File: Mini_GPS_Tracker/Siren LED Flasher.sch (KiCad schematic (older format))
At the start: 16 parts, among them IC3 MIC2288YML-TR, J6 Siren 12V, Q2 2N2219

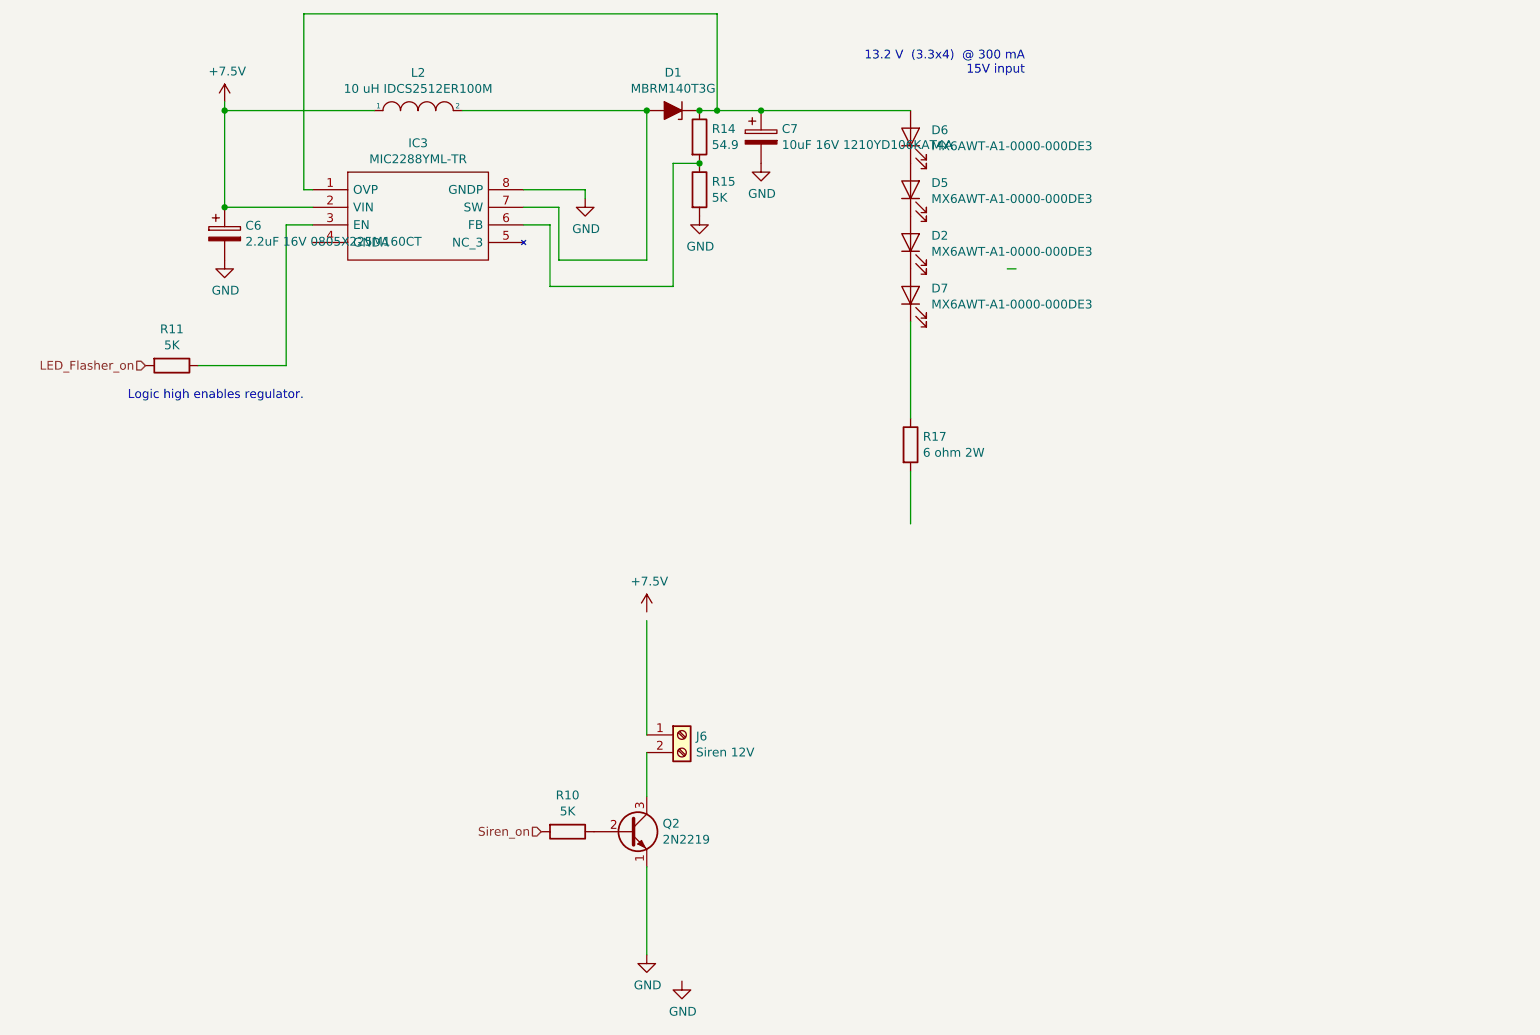
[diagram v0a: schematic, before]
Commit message: Add files via upload
More changes - USB, WiFi/BT, Buzzer, Siren-LED Flasher
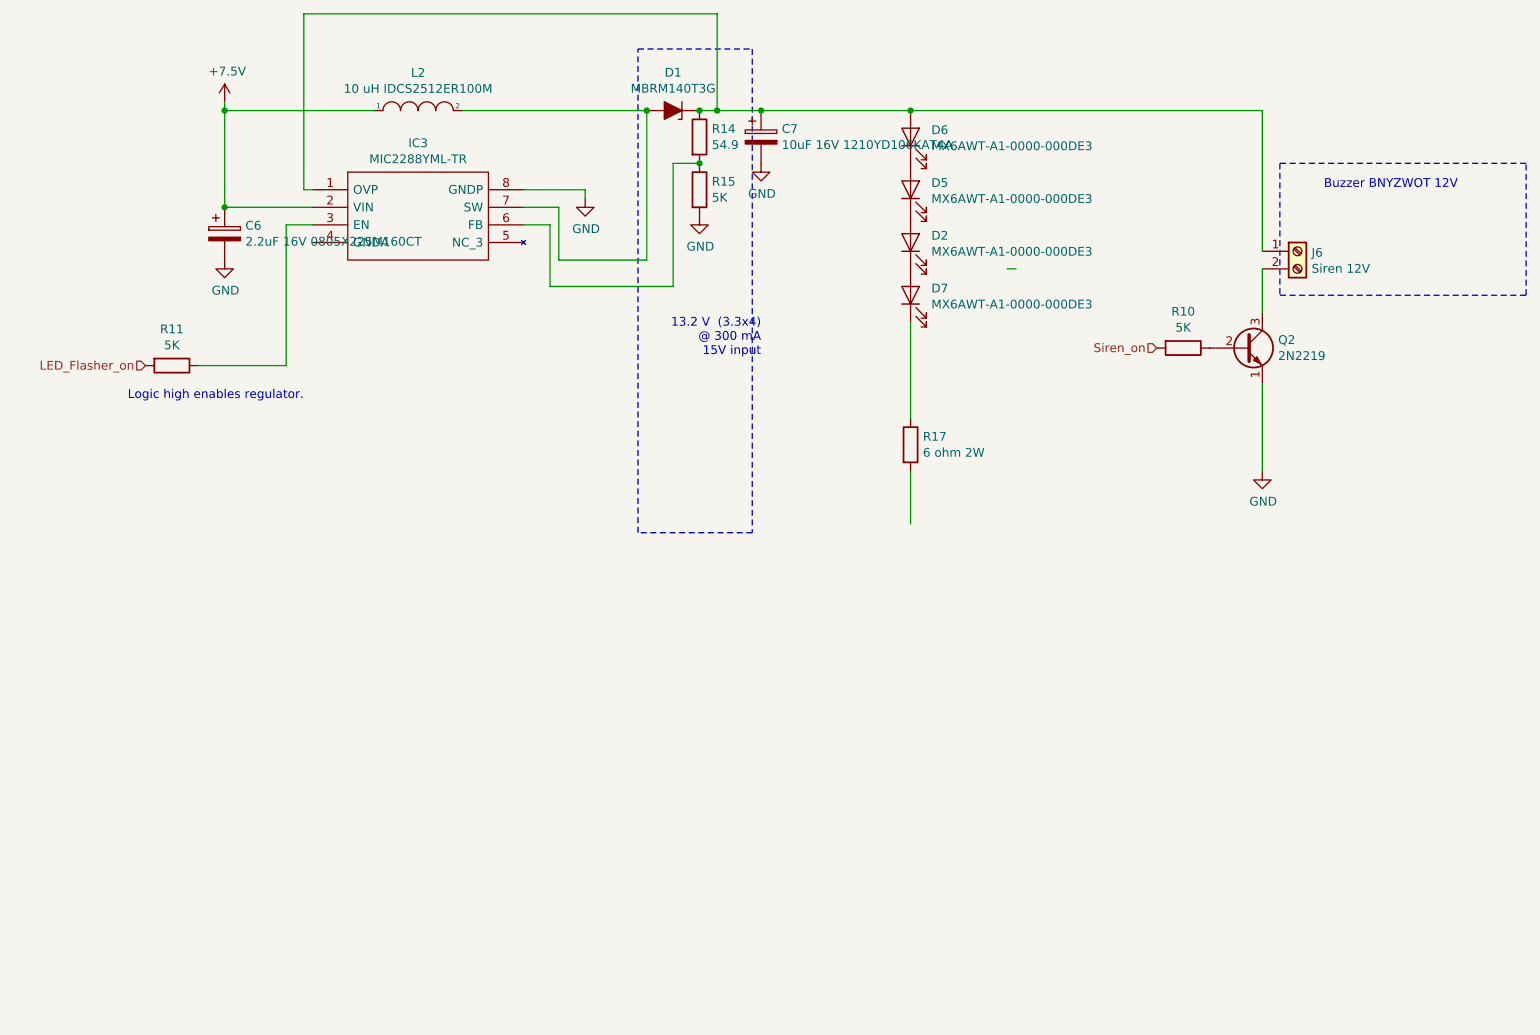
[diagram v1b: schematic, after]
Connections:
- wire segments 32 -> 33
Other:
- note added: "13.2 V (3.3x4) \n@ 300 mA\n15V input"
- note added: "Buzzer BNYZWOT 12V"
- note removed: "13.2 V (3.3x4) @ 300 mA\n15V input"
- moved on the sheet: J6, Q2, R10
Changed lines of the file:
@@
 Comment4 ""
 $EndDescr
-Text HLabel 5000 6000 0    50   Input ~ 0
+Text HLabel 8500 3250 0    50   Input ~ 0
 Siren_on
 Text HLabel 2750 3350 0    50   Input ~ 0
@@
 	1    4300 1900
 	1    0    0    -1
-$EndComp
-$Comp
-L Device:D_Zener_ALT D1
-U 1 1 5EB4CEF1
-P 5750 1900
-F 0 "D1" H 5750 1684 50  0000 C CNN
-F 1 "MBRM140T3G" H 5750 1775 50  0000 C CNN
-F 2 "" H 5750 1900 50  0001 C CNN
-F 3 "~" H 5750 1900 50  0001 C CNN
-	1    5750 1900
-	-1   0    0    1
 $EndComp
 $Comp
@@
 	5600 2750 5600 1900
 Wire Wire Line
-	5600 1900 4550 1900
-Wire Wire Line
 	3200 2450 3200 1900
 Wire Wire Line
 	3200 1900 4050 1900
-Connection ~ 5600 1900
-$Comp
-L Device:R R14
-U 1 1 5EB577A0
-P 5900 2050
-F 0 "R14" H 5970 2096 50  0000 L CNN
-F 1 "54.9" H 5970 2005 50  0000 L CNN
-F 2 "" V 5830 2050 50  0001 C CNN
-F 3 "~" H 5900 2050 50  0001 C CNN
-	1    5900 2050
-	1    0    0    -1
-$EndComp
-$Comp
-L Device:R R15
-U 1 1 5EB59096
-P 5900 2350
-F 0 "R15" H 5970 2396 50  0000 L CNN
-F 1 "5K" H 5970 2305 50  0000 L CNN
-F 2 "" V 5830 2350 50  0001 C CNN
-F 3 "~" H 5900 2350 50  0001 C CNN
-	1    5900 2350
-	1    0    0    -1
-$EndComp
-$Comp
-L power:GND #PWR060
-U 1 1 5EB59319
-P 5900 2500
-F 0 "#PWR060" H 5900 2250 50  0001 C CNN
-F 1 "GND" H 5905 2327 50  0000 C CNN
-F 2 "" H 5900 2500 50  0001 C CNN
-F 3 "" H 5900 2500 50  0001 C CNN
-	1    5900 2500
-	1    0    0    -1
-$EndComp
 Wire Wire Line
 	4900 2550 5050 2550
@@
 	5750 2900 5750 2200
 Wire Wire Line
-	5750 2200 5900 2200
-Connection ~ 5900 2200
-Wire Wire Line
 	5900 1900 6000 1900
-Connection ~ 5900 1900
 $Comp
 L Device:CP C6
@@
 	0    -1   -1   0
 $EndComp
-Text Notes 7750 1700 2    50   ~ 0
-13.2 V  (3.3x4)  @ 300 mA\n15V input
+Text Notes 6250 3300 2    50   ~ 0
+13.2 V  (3.3x4)  \n@ 300 mA\n15V input
 $Comp
 L Connector:Screw_Terminal_01x02 J6
 U 1 1 5EB7C544
-P 5800 5450
-F 0 "J6" H 5880 5442 50  0000 L CNN
-F 1 "Siren 12V" H 5880 5351 50  0000 L CNN
-F 2 "" H 5800 5450 50  0001 C CNN
-F 3 "~" H 5800 5450 50  0001 C CNN
-	1    5800 5450
+P 9300 2700
+F 0 "J6" H 9380 2692 50  0000 L CNN
+F 1 "Siren 12V" H 9380 2601 50  0000 L CNN
+F 2 "" H 9300 2700 50  0001 C CNN
+F 3 "~" H 9300 2700 50  0001 C CNN
+	1    9300 2700
 	1    0    0    -1
 $EndComp
@@
 	3650 1350 3650 2350
 $Comp
-L power:GND #PWR063
-U 1 1 5EB84950
-P 5800 6850
-F 0 "#PWR063" H 5800 6600 50  0001 C CNN
-F 1 "GND" H 5805 6677 50  0000 C CNN
-F 2 "" H 5800 6850 50  0001 C CNN
-F 3 "" H 5800 6850 50  0001 C CNN
-	1    5800 6850
-	1    0    0    -1
-$EndComp
-$Comp
 L Device:R R10
 U 1 1 5EB9F7A7
-P 5150 6000
-F 0 "R10" V 4943 6000 50  0000 C CNN
-F 1 "5K" V 5034 6000 50  0000 C CNN
-F 2 "" V 5080 6000 50  0001 C CNN
-F 3 "~" H 5150 6000 50  0001 C CNN
-	1    5150 6000
+P 8650 3250
+F 0 "R10" V 8443 3250 50  0000 C CNN
+F 1 "5K" V 8534 3250 50  0000 C CNN
+F 2 "" V 8580 3250 50  0001 C CNN
+F 3 "~" H 8650 3250 50  0001 C CNN
+	1    8650 3250
 	0    1    1    0
 $EndComp
@@
 L Transistor_BJT:2N2219 Q2
 U 1 1 5EBBDCB1
-P 5500 6000
-F 0 "Q2" H 5690 6046 50  0000 L CNN
-F 1 "2N2219" H 5690 5955 50  0000 L CNN
-F 2 "Package_TO_SOT_THT:TO-39-3" H 5700 5925 50  0001 L CIN
-F 3 "http://www.onsemi.com/pub_link/Collateral/2N2219-D.PDF" H 5500 6000 50  0001 L CNN
-	1    5500 6000
-	1    0    0    -1
-$EndComp
-Wire Wire Line
-	5600 4800 5600 5450
-Wire Wire Line
-	5600 5550 5600 5800
+P 9000 3250
+F 0 "Q2" H 9190 3296 50  0000 L CNN
+F 1 "2N2219" H 9190 3205 50  0000 L CNN
+F 2 "Package_TO_SOT_THT:TO-39-3" H 9200 3175 50  0001 L CIN
+F 3 "http://www.onsemi.com/pub_link/Collateral/2N2219-D.PDF" H 9000 3250 50  0001 L CNN
+	1    9000 3250
+	1    0    0    -1
+$EndComp
+Wire Wire Line
+	9100 2800 9100 3050
 Wire Wire Line
 	7100 3100 7100 3650
-$Comp
-L power:+7.5V #PWR053
-U 1 1 5EBC5061
-P 5600 4750
-F 0 "#PWR053" H 5600 4600 50  0001 C CNN
-F 1 "+7.5V" H 5615 4923 50  0000 C CNN
-F 2 "" H 5600 4750 50  0001 C CNN
-F 3 "" H 5600 4750 50  0001 C CNN
-	1    5600 4750
-	1    0    0    -1
-$EndComp
 $Comp
 L power:GND #PWR054
 U 1 1 5EBC5759
-P 5600 6700
-F 0 "#PWR054" H 5600 6450 50  0001 C CNN
-F 1 "GND" H 5605 6527 50  0000 C CNN
-F 2 "" H 5600 6700 50  0001 C CNN
-F 3 "" H 5600 6700 50  0001 C CNN
-	1    5600 6700
-	1    0    0    -1
-$EndComp
-Wire Wire Line
-	5600 6200 5600 6700
+P 9100 3950
+F 0 "#PWR054" H 9100 3700 50  0001 C CNN
+F 1 "GND" H 9105 3777 50  0000 C CNN
+F 2 "" H 9100 3950 50  0001 C CNN
+F 3 "" H 9100 3950 50  0001 C CNN
+	1    9100 3950
+	1    0    0    -1
+$EndComp
+Wire Wire Line
+	9100 3450 9100 3950
+Connection ~ 5900 1900
+Connection ~ 5600 1900
+Wire Wire Line
+	5600 1900 4550 1900
+Connection ~ 5900 2200
+Wire Wire Line
+	5750 2200 5900 2200
+$Comp
+L power:GND #PWR060
+U 1 1 5EB59319
+P 5900 2500
+F 0 "#PWR060" H 5900 2250 50  0001 C CNN
+F 1 "GND" H 5905 2327 50  0000 C CNN
+F 2 "" H 5900 2500 50  0001 C CNN
+F 3 "" H 5900 2500 50  0001 C CNN
+	1    5900 2500
+	1    0    0    -1
+$EndComp
+$Comp
+L Device:R R15
+U 1 1 5EB59096
+P 5900 2350
+F 0 "R15" H 5970 2396 50  0000 L CNN
+F 1 "5K" H 5970 2305 50  0000 L CNN
+F 2 "" V 5830 2350 50  0001 C CNN
+F 3 "~" H 5900 2350 50  0001 C CNN
+	1    5900 2350
+	1    0    0    -1
+$EndComp
+$Comp
+L Device:R R14
+U 1 1 5EB577A0
+P 5900 2050
+F 0 "R14" H 5970 2096 50  0000 L CNN
+F 1 "54.9" H 5970 2005 50  0000 L CNN
+F 2 "" V 5830 2050 50  0001 C CNN
+F 3 "~" H 5900 2050 50  0001 C CNN
+	1    5900 2050
+	1    0    0    -1
+$EndComp
+$Comp
+L Device:D_Zener_ALT D1
+U 1 1 5EB4CEF1
+P 5750 1900
+F 0 "D1" H 5750 1684 50  0000 C CNN
+F 1 "MBRM140T3G" H 5750 1775 50  0000 C CNN
+F 2 "" H 5750 1900 50  0001 C CNN
+F 3 "~" H 5750 1900 50  0001 C CNN
+	1    5750 1900
+	-1   0    0    1
+$EndComp
+Wire Notes Line
+	6200 1550 6200 4300
+Wire Notes Line
+	6200 4300 5550 4300
+Wire Notes Line
+	5550 4300 5550 1550
+Wire Notes Line
+	5550 1550 6200 1550
+Wire Notes Line
+	9200 2950 10600 2950
+Wire Notes Line
+	10600 2950 10600 2200
+Wire Notes Line
+	10600 2200 9200 2200
+Wire Notes Line
+	9200 2200 9200 2950
+Text Notes 9450 2350 0    50   ~ 0
+Buzzer BNYZWOT 12V
+Wire Wire Line
+	7100 1900 9100 1900
+Wire Wire Line
+	9100 1900 9100 2700
+Connection ~ 7100 1900
 $EndSCHEMATC
